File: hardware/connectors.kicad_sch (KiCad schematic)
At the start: 24 parts, among them J1 Kenwood-2.5, J10 UART, J11 Radio_Opt, J12 Speaker, J13 KH-RJ45-58-8P8C, J2 USB_C, J301 +12V, J301 OLED, J5 Kenwood-3.5, J7 Radio, J9 STLink, U3 USBLC6-2

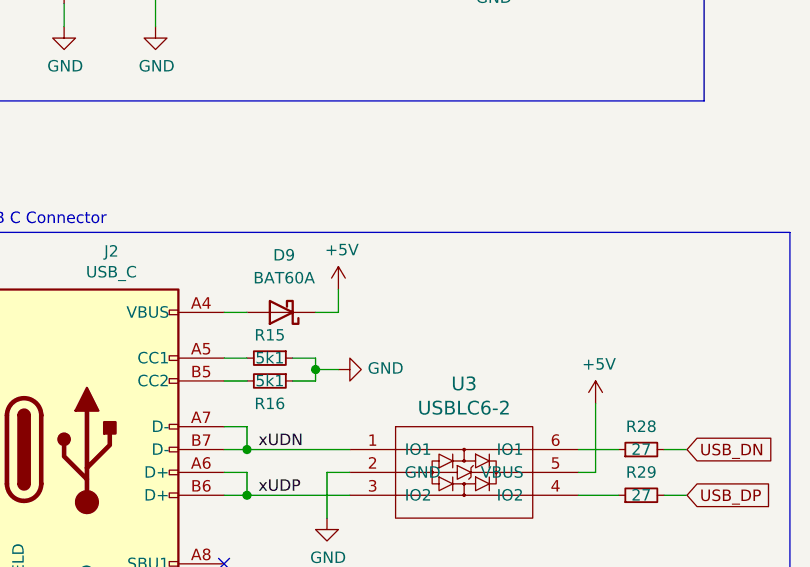
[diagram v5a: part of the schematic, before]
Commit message: Updated power supply filters
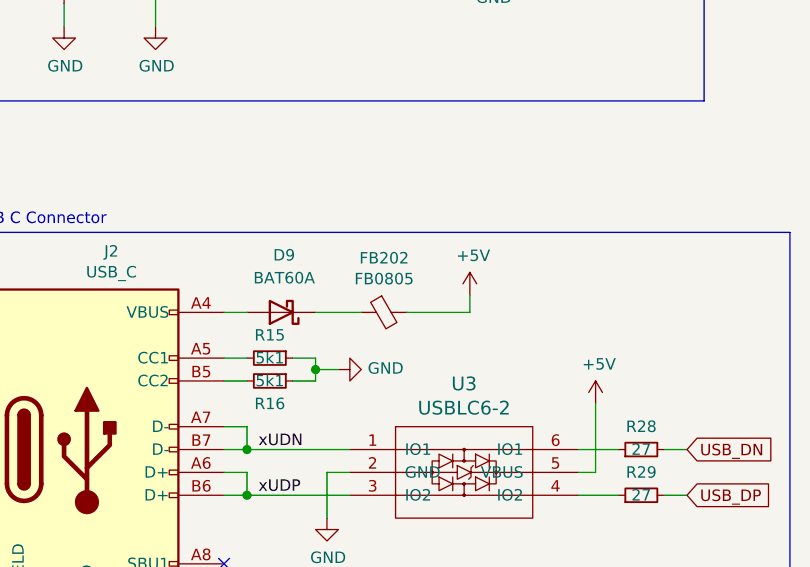
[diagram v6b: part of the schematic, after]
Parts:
- added FB202: FB0805, pkl_dipol:L_0805, symbol Device:Ferrite_Bead_Small
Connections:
- net +5V: now also FB202.2; no longer D9.1 (K)
- new net: D9.1 (K), FB202.1
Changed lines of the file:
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@@
     (stroke (width 0) (type solid))
   )
-  (wire (pts (xy 60.96 95.885) (xy 63.5 95.885))
+  (wire (pts (xy 60.96 95.885) (xy 66.04 95.885))
     (stroke (width 0) (type solid))
   )
@@
     (stroke (width 0) (type solid))
   )
+  (wire (pts (xy 71.12 95.885) (xy 78.105 95.885))
+    (stroke (width 0) (type default))
+  )
   (wire (pts (xy 250.19 44.45) (xy 250.19 46.355))
     (stroke (width 0) (type default))
@@
     (stroke (width 0) (type solid))
   )
+  (wire (pts (xy 78.105 93.98) (xy 78.105 95.885))
+    (stroke (width 0) (type default))
+  )
   (wire (pts (xy 62.23 113.665) (xy 62.23 118.745))
     (stroke (width 0) (type solid))
@@
   (wire (pts (xy 40.64 48.895) (xy 43.18 48.895))
     (stroke (width 0) (type default))
-  )
-  (wire (pts (xy 63.5 95.885) (xy 63.5 93.345))
-    (stroke (width 0) (type solid))
   )
   (wire (pts (xy 196.215 113.665) (xy 203.835 113.665))
@@
     )
   )
-  (symbol (lib_id "power:+5V") (at 63.5 93.345 0) (unit 1)
-    (in_bom yes) (on_board yes) (dnp no)
-    (property "Reference" "#PWR048" (at 63.5 97.155 0)
-      (effects (font (size 1.27 1.27)) hide)
-    )
-    (property "Value" "+5V" (at 63.881 88.9508 0)
-      (effects (font (size 1.27 1.27)))
-    )
-    (property "Footprint" "" (at 63.5 93.345 0)
-      (effects (font (size 1.27 1.27)) hide)
-    )
-    (property "Datasheet" "" (at 63.5 93.345 0)
-      (effects (font (size 1.27 1.27)) hide)
-    )
-    (pin "1")
-    (instances
-      (project "M17-SmartMic"
-        (path "/59592280-3207-432b-a891-cd517ec5cf12/00000000-0000-0000-0000-0000612c95ef"
-          (reference "#PWR048") (unit 1)
-        )
-        (path "/59592280-3207-432b-a891-cd517ec5cf12/7f9420e4-5dd1-4e05-8205-18dae2029540"
-          (reference "#PWR0406") (unit 1)
-        )
-      )
-    )
-  )
   (symbol (lib_id "pkl_device:pkl_C_Small") (at 153.035 111.76 0) (unit 1)
     (in_bom yes) (on_board yes) (dnp no)
@@
         (path "/59592280-3207-432b-a891-cd517ec5cf12/7f9420e4-5dd1-4e05-8205-18dae2029540"
           (reference "#PWR0421") (unit 1)
+        )
+      )
+    )
+  )
+  (symbol (lib_id "Device:Ferrite_Bead_Small") (at 68.58 95.885 90) (mirror x) (unit 1)
+    (in_bom yes) (on_board yes) (dnp no)
+    (property "Reference" "FB202" (at 68.58 89.8652 90)
+      (effects (font (size 1.27 1.27)))
+    )
+    (property "Value" "FB0805" (at 68.58 92.1766 90)
+      (effects (font (size 1.27 1.27)))
+    )
+    (property "Footprint" "pkl_dipol:L_0805" (at 68.58 94.107 90)
+      (effects (font (size 1.27 1.27)) hide)
+    )
+    (property "Datasheet" "~" (at 68.58 95.885 0)
+      (effects (font (size 1.27 1.27)) hide)
+    )
+    (property "MPN" "2508056017Y2" (at 68.58 95.885 0)
+      (effects (font (size 1.27 1.27)) hide)
+    )
+    (property "LCSC Part #" "C1017" (at 68.58 95.885 0)
+      (effects (font (size 1.27 1.27)) hide)
+    )
+    (pin "1")
+    (pin "2")
+    (instances
+      (project "M17-SmartMic"
+        (path "/59592280-3207-432b-a891-cd517ec5cf12/00000000-0000-0000-0000-0000612c95ef"
+          (reference "FB202") (unit 1)
+        )
+        (path "/59592280-3207-432b-a891-cd517ec5cf12/7f9420e4-5dd1-4e05-8205-18dae2029540"
+          (reference "FB401") (unit 1)
         )
       )
@@
         )
       )
+    )
+  )
+  (symbol (lib_id "power:+5V") (at 78.105 93.98 0) (unit 1)
+    (in_bom yes) (on_board yes) (dnp no)
+    (property "Reference" "#PWR048" (at 78.105 97.79 0)
+      (effects (font (size 1.27 1.27)) hide)
+    )
+    (property "Value" "+5V" (at 78.486 89.5858 0)
+      (effects (font (size 1.27 1.27)))
+    )
+    (property "Footprint" "" (at 78.105 93.98 0)
+      (effects (font (size 1.27 1.27)) hide)
+    )
+    (property "Datasheet" "" (at 78.105 93.98 0)
+      (effects (font (size 1.27 1.27)) hide)
+    )
+    (pin "1")
+    (instances
+      (project "M17-SmartMic"
+        (path "/59592280-3207-432b-a891-cd517ec5cf12/00000000-0000-0000-0000-0000612c95ef"
+          (reference "#PWR048") (unit 1)
+        )
+        (path "/59592280-3207-432b-a891-cd517ec5cf12/7f9420e4-5dd1-4e05-8205-18dae2029540"
+          (reference "#PWR0406") (unit 1)
+        )
+      )

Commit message: PCB Layout [WIP]
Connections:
- net +5V: now also FB202.1; no longer FB202.2
- net at D9.1 (K): now also FB202.2; no longer FB202.1
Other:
- moved on the sheet: FB202
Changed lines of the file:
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@@
     )
   )
-  (symbol (lib_id "Device:Ferrite_Bead_Small") (at 68.58 95.885 90) (mirror x) (unit 1)
+  (symbol (lib_id "Device:Ferrite_Bead_Small") (at 68.58 95.885 270) (unit 1)
     (in_bom yes) (on_board yes) (dnp no)
     (property "Reference" "FB202" (at 68.58 89.8652 90)

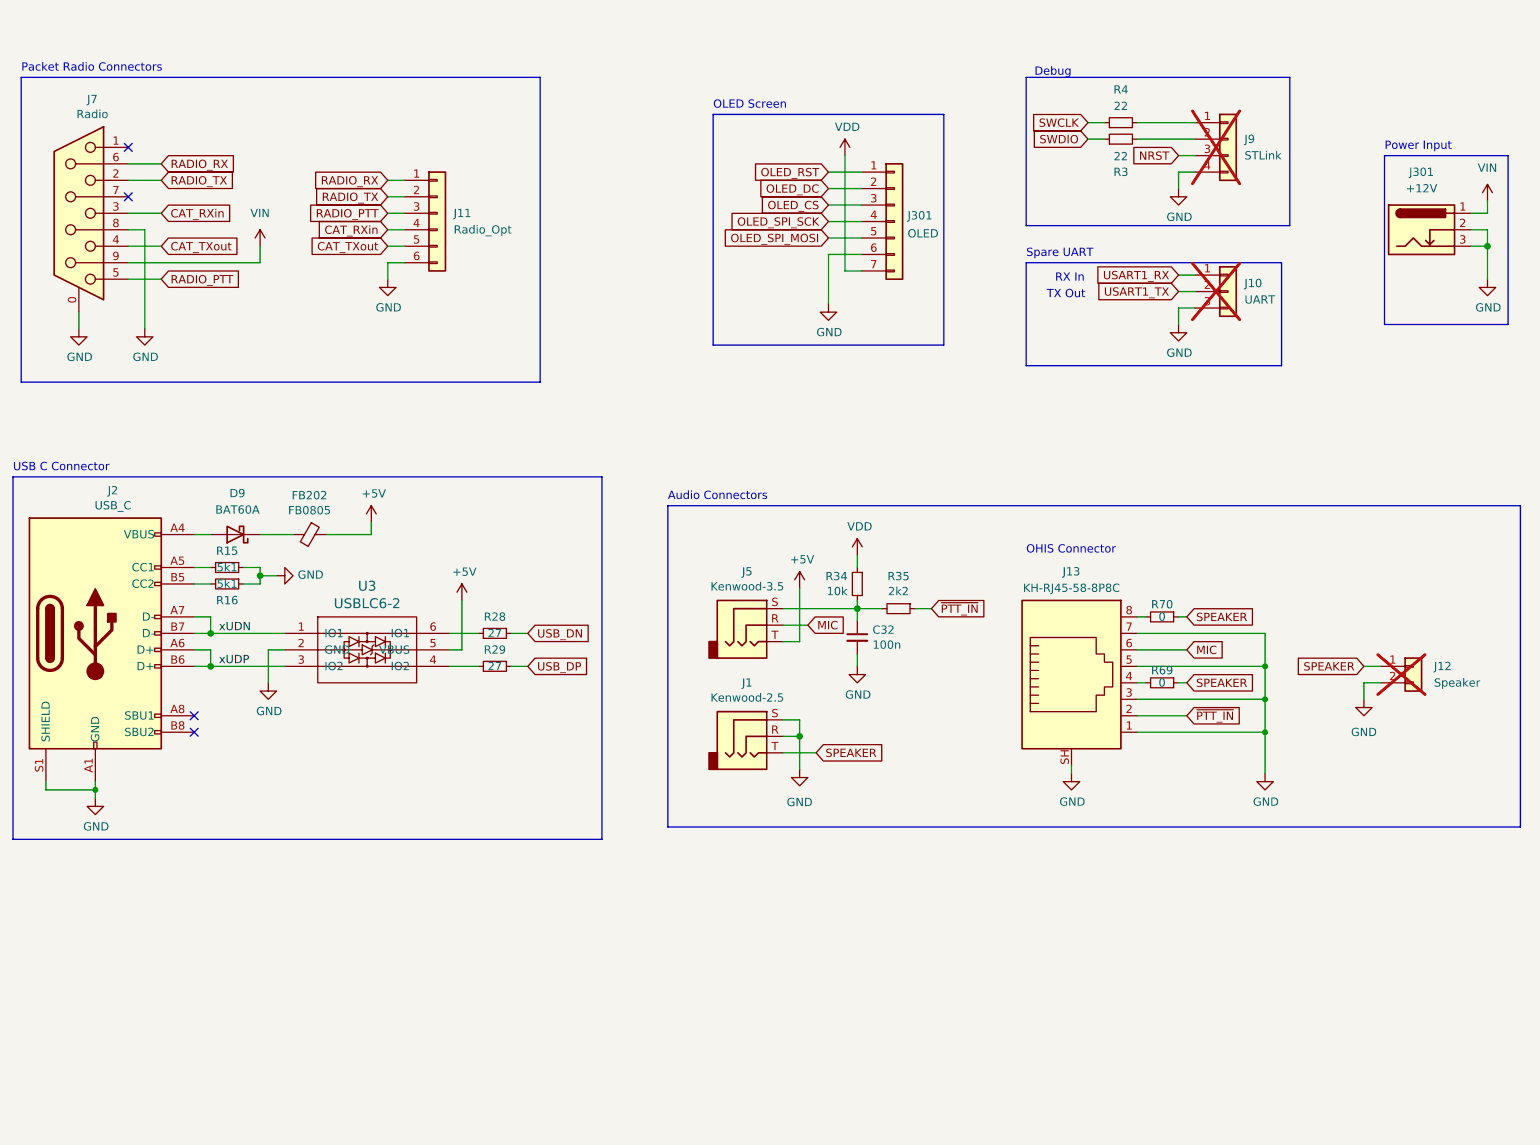
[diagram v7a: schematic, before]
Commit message: PCB Layout [WIP] + HMI connector
Added ZIF connector for HMI, updated reset button reference, added backup power connector for RTC + general layout progress
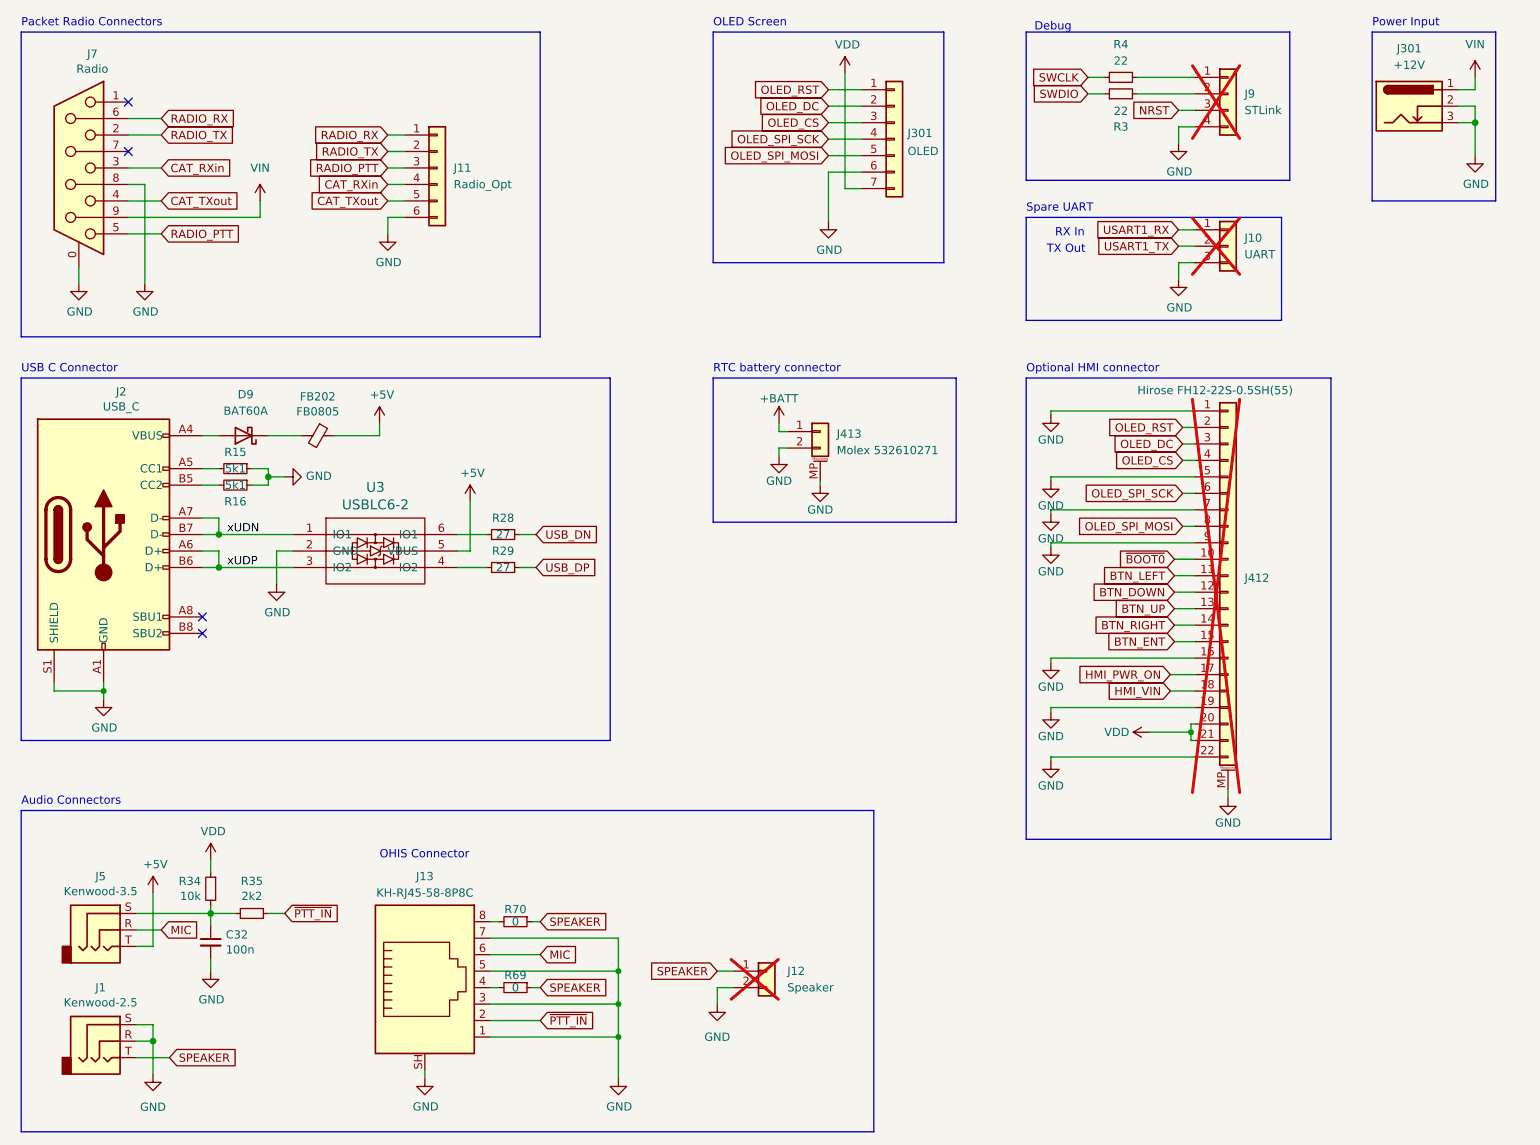
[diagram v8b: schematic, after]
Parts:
- added J412: Hirose FH12-22S-0.5SH(55), Connector_FFC-FPC:Hirose_FH12-22S-0.5SH_1x22-1MP_P0.50mm_Horizontal, symbol Connector_Generic_MountingPin:Conn_01x22_MountingPin
- added J413: Molex 532610271, Connector_Molex:Molex_PicoBlade_53261-0271_1x02-1MP_P1.25mm_Horizontal, symbol Connector_Generic_MountingPin:Conn_01x02_MountingPin
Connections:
- net GND: now also J412.1 (Pin_1), J412.16 (Pin_16), J412.19 (Pin_19), J412.22 (Pin_22), J412.5 (Pin_5), J412.7 (Pin_7), J412.9 (Pin_9), J412.MP (MountPin), J413.2 (Pin_2), J413.MP (MountPin)
- net OLED_CS: now also J412.4 (Pin_4)
- net OLED_DC: now also J412.3 (Pin_3)
- net OLED_RST: now also J412.2 (Pin_2)
- net OLED_SPI_MOSI: now also J412.8 (Pin_8)
- net OLED_SPI_SCK: now also J412.6 (Pin_6)
- net VDD: now also J412.20 (Pin_20), J412.21 (Pin_21)
- new net +BATT: J413.1 (Pin_1)
- new net BTN_DOWN: J412.12 (Pin_12)
- new net BTN_ENT: J412.15 (Pin_15)
- new net BTN_LEFT: J412.11 (Pin_11)
- new net BTN_RIGHT: J412.14 (Pin_14)
- new net BTN_UP: J412.13 (Pin_13)
- new net HMI_PWR_ON: J412.17 (Pin_17)
- new net HMI_VIN: J412.18 (Pin_18)
- new net ~{BOOT0}: J412.10 (Pin_10)
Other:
- note added: "Optional HMI connector"
- note added: "RTC battery connector"
- moved on the sheet: C32, D9, FB202, J1, J10, J11, J12, J13, J2, J301, J5, J7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
